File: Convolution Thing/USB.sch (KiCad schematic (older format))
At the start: 4 parts

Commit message: Added gate inputs and CM4 / display sockets, made CV inputs 100k, lots of smaller changes. First iteration of schematic now done.
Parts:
- removed J?: USB_C_Receptacle_USB2.0, symbol Connector:USB_C_Receptacle_USB2.0
- removed R? (x2): 56k, symbol Device:R
- added C?: 100nF, symbol Device:C
- added J?: USB_A, symbol Connector:USB_A
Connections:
- net labels removed: CC1, CC2
- wire segments 8 -> 4
- no-connect marks 2 -> 0
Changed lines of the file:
@@
 $Descr A4 11693 8268
 encoding utf-8
-Sheet 11 11
+Sheet 11 13
 Title ""
 Date ""
@@
 	1    0    0    -1
 $EndComp
-$Comp
-L Connector:USB_C_Receptacle_USB2.0 J?
-U 1 1 6120E9FA
-P 1400 2700
-F 0 "J?" H 1507 3567 50  0000 C CNN
-F 1 "USB_C_Receptacle_USB2.0" H 1507 3476 50  0000 C CNN
-F 2 "" H 1550 2700 50  0001 C CNN
-F 3 "https://www.usb.org/sites/default/files/documents/usb_type-c.zip" H 1550 2700 50  0001 C CNN
-	1    1400 2700
-	1    0    0    -1
-$EndComp
-$Comp
-L power:GND #PWR?
-U 1 1 61212A3C
-P 1400 3600
-F 0 "#PWR?" H 1400 3350 50  0001 C CNN
-F 1 "GND" H 1405 3427 50  0000 C CNN
-F 2 "" H 1400 3600 50  0001 C CNN
-F 3 "" H 1400 3600 50  0001 C CNN
-	1    1400 3600
-	1    0    0    -1
-$EndComp
-$Comp
-L power:GND #PWR?
-U 1 1 61213DAD
-P 1100 3600
-F 0 "#PWR?" H 1100 3350 50  0001 C CNN
-F 1 "GND" H 1105 3427 50  0000 C CNN
-F 2 "" H 1100 3600 50  0001 C CNN
-F 3 "" H 1100 3600 50  0001 C CNN
-	1    1100 3600
-	1    0    0    -1
-$EndComp
 Text Label 1800 1200 0    50   ~ 0
 USB_N
 Text Label 1800 1300 0    50   ~ 0
 USB_P
-Wire Wire Line
-	2000 2700 2000 2600
-Wire Wire Line
-	2000 2800 2000 2900
-Text Label 2100 2600 0    50   ~ 0
-USB_N
-Wire Wire Line
-	2100 2600 2000 2600
-Connection ~ 2000 2600
-Text Label 2100 2800 0    50   ~ 0
-USB_P
-Wire Wire Line
-	2100 2800 2000 2800
-Connection ~ 2000 2800
-Text Label 2000 2100 0    50   ~ 0
-VBUS
-Text Label 3200 1500 0    50   ~ 0
+Text Label 3250 1000 2    50   ~ 0
 VBUS
 $Comp
 L power:+5V #PWR?
 U 1 1 61219689
-P 3200 1100
-F 0 "#PWR?" H 3200 950 50  0001 C CNN
-F 1 "+5V" H 3215 1273 50  0000 C CNN
-F 2 "" H 3200 1100 50  0001 C CNN
-F 3 "" H 3200 1100 50  0001 C CNN
-	1    3200 1100
-	1    0    0    -1
-$EndComp
-Text Label 2000 2300 0    50   ~ 0
-CC1
-Text Label 2000 2400 0    50   ~ 0
-CC2
-Text Label 3650 1500 0    50   ~ 0
-CC1
-$Comp
-L Device:R R?
-U 1 1 6121C44A
-P 3650 1250
-F 0 "R?" H 3720 1296 50  0000 L CNN
-F 1 "56k" V 3650 1200 50  0000 L CNN
-F 2 "" V 3580 1250 50  0001 C CNN
-F 3 "~" H 3650 1250 50  0001 C CNN
-	1    3650 1250
+P 3650 1000
+F 0 "#PWR?" H 3650 850 50  0001 C CNN
+F 1 "+5V" H 3665 1173 50  0000 C CNN
+F 2 "" H 3650 1000 50  0001 C CNN
+F 3 "" H 3650 1000 50  0001 C CNN
+	1    3650 1000
 	1    0    0    -1
 $EndComp
 Wire Wire Line
-	3650 1500 3650 1400
-Wire Wire Line
 	2750 1000 2750 1400
-Wire Wire Line
-	3200 1100 3200 1500
 $Comp
-L power:+5V #PWR?
-U 1 1 6121D644
-P 3650 1100
-F 0 "#PWR?" H 3650 950 50  0001 C CNN
-F 1 "+5V" H 3665 1273 50  0000 C CNN
-F 2 "" H 3650 1100 50  0001 C CNN
-F 3 "" H 3650 1100 50  0001 C CNN
-	1    3650 1100
+L Connector:USB_A J?
+U 1 1 610E4AAF
+P 1200 2300
+F 0 "J?" H 1257 2767 50  0000 C CNN
+F 1 "USB_A" H 1257 2676 50  0000 C CNN
+F 2 "" H 1350 2250 50  0001 C CNN
+F 3 " ~" H 1350 2250 50  0001 C CNN
+	1    1200 2300
 	1    0    0    -1
 $EndComp
-Text Label 4100 1500 0    50   ~ 0
-CC2
+Text Label 1500 2100 0    50   ~ 0
+VBUS
+Text Label 1500 2300 0    50   ~ 0
+USB_P
+Text Label 1500 2400 0    50   ~ 0
+USB_N
 $Comp
-L Device:R R?
-U 1 1 6121EAE8
-P 4100 1250
-F 0 "R?" H 4170 1296 50  0000 L CNN
-F 1 "56k" V 4100 1200 50  0000 L CNN
-F 2 "" V 4030 1250 50  0001 C CNN
-F 3 "~" H 4100 1250 50  0001 C CNN
-	1    4100 1250
+L power:GND #PWR?
+U 1 1 610E6611
+P 1200 2700
+F 0 "#PWR?" H 1200 2450 50  0001 C CNN
+F 1 "GND" H 1205 2527 50  0000 C CNN
+F 2 "" H 1200 2700 50  0001 C CNN
+F 3 "" H 1200 2700 50  0001 C CNN
+	1    1200 2700
 	1    0    0    -1
 $EndComp
 Wire Wire Line
-	4100 1500 4100 1400
+	1200 2700 1100 2700
+Connection ~ 1200 2700
 $Comp
-L power:+5V #PWR?
-U 1 1 6121EAEF
-P 4100 1100
-F 0 "#PWR?" H 4100 950 50  0001 C CNN
-F 1 "+5V" H 4115 1273 50  0000 C CNN
-F 2 "" H 4100 1100 50  0001 C CNN
-F 3 "" H 4100 1100 50  0001 C CNN
-	1    4100 1100
+L Device:C C?
+U 1 1 612D057E
+P 3450 1150
+F 0 "C?" H 3565 1196 50  0000 L CNN
+F 1 "100nF" H 3565 1105 50  0000 L CNN
+F 2 "" H 3488 1000 50  0001 C CNN
+F 3 "~" H 3450 1150 50  0001 C CNN
+	1    3450 1150
 	1    0    0    -1
 $EndComp
-NoConn ~ 2000 3200
-NoConn ~ 2000 3300
+Wire Wire Line
+	3450 1000 3650 1000
+Wire Wire Line
+	3450 1000 3250 1000
+Connection ~ 3450 1000
+$Comp
+L power:GND #PWR?
+U 1 1 612D0E27
+P 3450 1300
+F 0 "#PWR?" H 3450 1050 50  0001 C CNN
+F 1 "GND" H 3455 1127 50  0000 C CNN
+F 2 "" H 3450 1300 50  0001 C CNN
+F 3 "" H 3450 1300 50  0001 C CNN
+	1    3450 1300
+	1    0    0    -1
+$EndComp
 $EndSCHEMATC

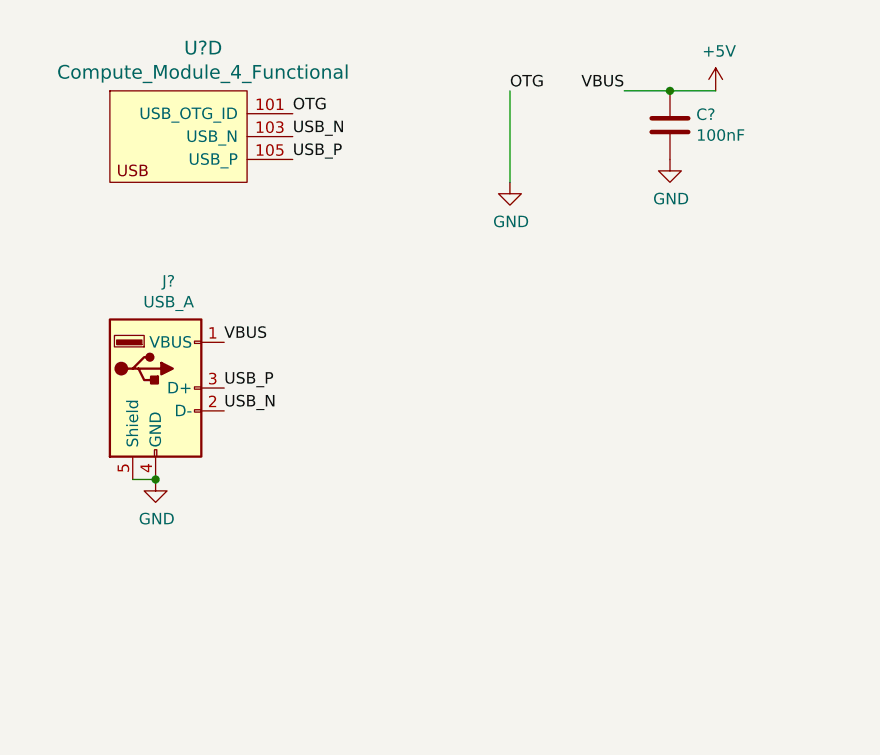
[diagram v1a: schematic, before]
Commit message: Fix some issues, add component references
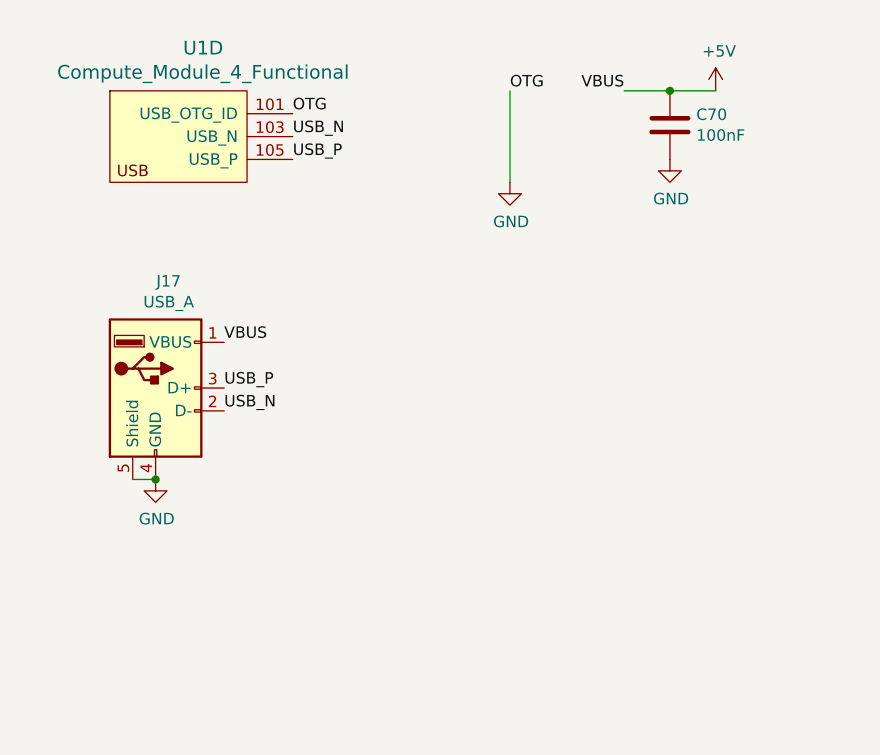
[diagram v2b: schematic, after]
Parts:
- gave numbers to parts that had none: 3
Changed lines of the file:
@@
 $EndDescr
 $Comp
-L CM4:Compute_Module_4_Functional U?
+L CM4:Compute_Module_4_Functional U1
 U 4 1 61202175
 P 800 1100
-F 0 "U?" H 1408 1387 60  0000 C CNN
+F 0 "U1" H 1408 1387 60  0000 C CNN
 F 1 "Compute_Module_4_Functional" H 1408 1281 60  0000 C CNN
 F 2 "" H 1000 1150 60  0001 L CNN
@@
 OTG
 $Comp
-L power:GND #PWR?
+L power:GND #PWR0127
 U 1 1 6120C5F8
 P 2750 1400
-F 0 "#PWR?" H 2750 1150 50  0001 C CNN
+F 0 "#PWR0127" H 2750 1150 50  0001 C CNN
 F 1 "GND" H 2755 1227 50  0000 C CNN
 F 2 "" H 2750 1400 50  0001 C CNN
@@
 VBUS
 $Comp
-L power:+5V #PWR?
+L power:+5V #PWR0129
 U 1 1 61219689
 P 3650 1000
-F 0 "#PWR?" H 3650 850 50  0001 C CNN
+F 0 "#PWR0129" H 3650 850 50  0001 C CNN
 F 1 "+5V" H 3665 1173 50  0000 C CNN
 F 2 "" H 3650 1000 50  0001 C CNN
@@
 	2750 1000 2750 1400
 $Comp
-L Connector:USB_A J?
+L Connector:USB_A J17
 U 1 1 610E4AAF
 P 1200 2300
-F 0 "J?" H 1257 2767 50  0000 C CNN
+F 0 "J17" H 1257 2767 50  0000 C CNN
 F 1 "USB_A" H 1257 2676 50  0000 C CNN
 F 2 "" H 1350 2250 50  0001 C CNN
@@
 USB_N
 $Comp
-L power:GND #PWR?
+L power:GND #PWR0126
 U 1 1 610E6611
 P 1200 2700
-F 0 "#PWR?" H 1200 2450 50  0001 C CNN
+F 0 "#PWR0126" H 1200 2450 50  0001 C CNN
 F 1 "GND" H 1205 2527 50  0000 C CNN
 F 2 "" H 1200 2700 50  0001 C CNN
@@
 Connection ~ 1200 2700
 $Comp
-L Device:C C?
+L Device:C C70
 U 1 1 612D057E
 P 3450 1150
-F 0 "C?" H 3565 1196 50  0000 L CNN
+F 0 "C70" H 3565 1196 50  0000 L CNN
 F 1 "100nF" H 3565 1105 50  0000 L CNN
 F 2 "" H 3488 1000 50  0001 C CNN
@@
 Connection ~ 3450 1000
 $Comp
-L power:GND #PWR?
+L power:GND #PWR0128
 U 1 1 612D0E27
 P 3450 1300
-F 0 "#PWR?" H 3450 1050 50  0001 C CNN
+F 0 "#PWR0128" H 3450 1050 50  0001 C CNN
 F 1 "GND" H 3455 1127 50  0000 C CNN
 F 2 "" H 3450 1300 50  0001 C CNN

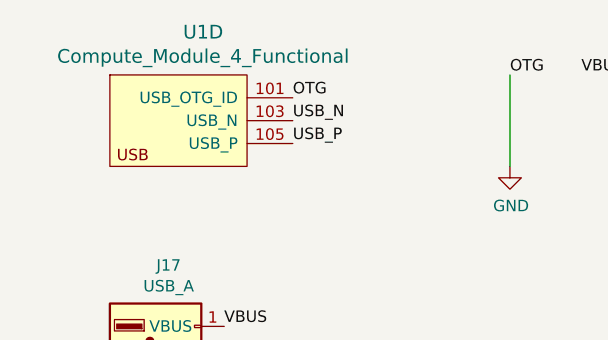
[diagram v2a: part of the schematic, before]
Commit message: Started footprint assignment
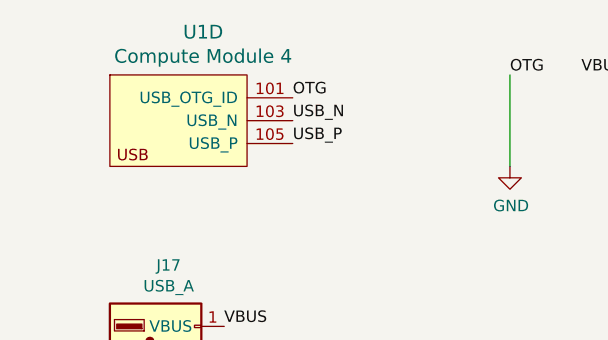
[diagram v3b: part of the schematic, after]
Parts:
- U1: value Compute_Module_4_Functional -> Compute Module 4; footprint (none) -> CM4:Raspberry-Pi-4-Compute-Module
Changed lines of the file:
@@
 P 800 1100
 F 0 "U1" H 1408 1387 60  0000 C CNN
-F 1 "Compute_Module_4_Functional" H 1408 1281 60  0000 C CNN
-F 2 "" H 1000 1150 60  0001 L CNN
+F 1 "Compute Module 4" H 1408 1281 60  0000 C CNN
+F 2 "CM4:Raspberry-Pi-4-Compute-Module" H 1000 1150 60  0001 L CNN
 F 3 "" H 1000 950 60  0001 L CNN
 	4    800  1100

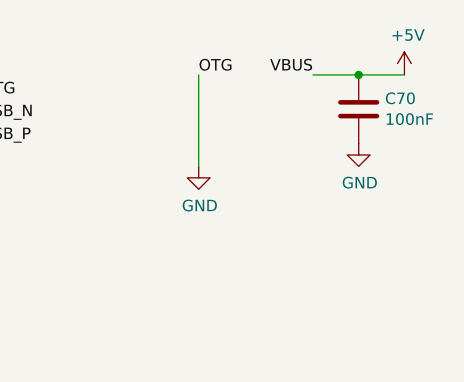
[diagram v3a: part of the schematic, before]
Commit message: Assign all footprints
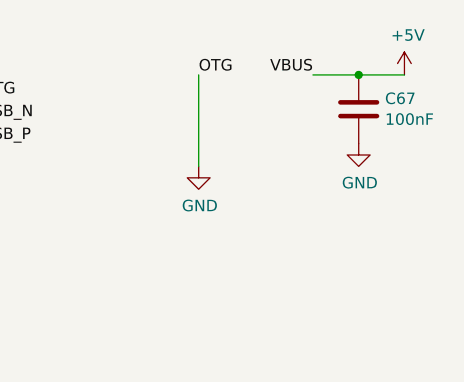
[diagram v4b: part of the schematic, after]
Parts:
- C67: renamed from C70; footprint (none) -> Capacitor_SMD:C_0805_2012Metric
- J17: footprint (none) -> Connector_USB:USB_A_Molex_105057_Vertical
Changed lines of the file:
@@
 OTG
 $Comp
-L power:GND #PWR0127
+L power:GND #PWR0120
 U 1 1 6120C5F8
 P 2750 1400
-F 0 "#PWR0127" H 2750 1150 50  0001 C CNN
+F 0 "#PWR0120" H 2750 1150 50  0001 C CNN
 F 1 "GND" H 2755 1227 50  0000 C CNN
 F 2 "" H 2750 1400 50  0001 C CNN
@@
 VBUS
 $Comp
-L power:+5V #PWR0129
+L power:+5V #PWR0122
 U 1 1 61219689
 P 3650 1000
-F 0 "#PWR0129" H 3650 850 50  0001 C CNN
+F 0 "#PWR0122" H 3650 850 50  0001 C CNN
 F 1 "+5V" H 3665 1173 50  0000 C CNN
 F 2 "" H 3650 1000 50  0001 C CNN
@@
 F 0 "J17" H 1257 2767 50  0000 C CNN
 F 1 "USB_A" H 1257 2676 50  0000 C CNN
-F 2 "" H 1350 2250 50  0001 C CNN
+F 2 "Connector_USB:USB_A_Molex_105057_Vertical" H 1350 2250 50  0001 C CNN
 F 3 " ~" H 1350 2250 50  0001 C CNN
 	1    1200 2300
@@
 USB_N
 $Comp
-L power:GND #PWR0126
+L power:GND #PWR0119
 U 1 1 610E6611
 P 1200 2700
-F 0 "#PWR0126" H 1200 2450 50  0001 C CNN
+F 0 "#PWR0119" H 1200 2450 50  0001 C CNN
 F 1 "GND" H 1205 2527 50  0000 C CNN
 F 2 "" H 1200 2700 50  0001 C CNN
@@
 Connection ~ 1200 2700
 $Comp
-L Device:C C70
+L Device:C C67
 U 1 1 612D057E
 P 3450 1150
-F 0 "C70" H 3565 1196 50  0000 L CNN
+F 0 "C67" H 3565 1196 50  0000 L CNN
 F 1 "100nF" H 3565 1105 50  0000 L CNN
-F 2 "" H 3488 1000 50  0001 C CNN
+F 2 "Capacitor_SMD:C_0805_2012Metric" H 3488 1000 50  0001 C CNN
 F 3 "~" H 3450 1150 50  0001 C CNN
 	1    3450 1150
@@
 Connection ~ 3450 1000
 $Comp
-L power:GND #PWR0128
+L power:GND #PWR0121
 U 1 1 612D0E27
 P 3450 1300
-F 0 "#PWR0128" H 3450 1050 50  0001 C CNN
+F 0 "#PWR0121" H 3450 1050 50  0001 C CNN
 F 1 "GND" H 3455 1127 50  0000 C CNN
 F 2 "" H 3450 1300 50  0001 C CNN

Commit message: PCB layout work and related changes to the schematic
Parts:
- removed U1: Compute Module 4, CM4:Raspberry-Pi-4-Compute-Module, symbol CM4:Compute_Module_4_Functional
- renumbered C67 to C64, J17 to J15
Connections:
- net USB_N renamed CM4_USB_N
- net USB_P renamed CM4_USB_P
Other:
- moved on the sheet: C64, J15
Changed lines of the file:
@@
 $Descr A4 11693 8268
 encoding utf-8
-Sheet 11 13
+Sheet 10 13
 Title ""
 Date ""
@@
 Comment4 ""
 $EndDescr
+Text Label 1850 1050 2    50   ~ 0
+VBUS
 $Comp
-L CM4:Compute_Module_4_Functional U1
-U 4 1 61202175
-P 800 1100
-F 0 "U1" H 1408 1387 60  0000 C CNN
-F 1 "Compute Module 4" H 1408 1281 60  0000 C CNN
-F 2 "CM4:Raspberry-Pi-4-Compute-Module" H 1000 1150 60  0001 L CNN
-F 3 "" H 1000 950 60  0001 L CNN
-	4    800  1100
+L power:+5V #PWR0112
+U 1 1 61219689
+P 2250 1050
+F 0 "#PWR0112" H 2250 900 50  0001 C CNN
+F 1 "+5V" H 2265 1223 50  0000 C CNN
+F 2 "" H 2250 1050 50  0001 C CNN
+F 3 "" H 2250 1050 50  0001 C CNN
+	1    2250 1050
 	1    0    0    -1
 $EndComp
-Text Label 1800 1100 0    50   ~ 0
-OTG
-Text Label 2750 1000 0    50   ~ 0
-OTG
 $Comp
-L power:GND #PWR0120
-U 1 1 6120C5F8
-P 2750 1400
-F 0 "#PWR0120" H 2750 1150 50  0001 C CNN
-F 1 "GND" H 2755 1227 50  0000 C CNN
-F 2 "" H 2750 1400 50  0001 C CNN
-F 3 "" H 2750 1400 50  0001 C CNN
-	1    2750 1400
+L Connector:USB_A J15
+U 1 1 610E4AAF
+P 950 1200
+F 0 "J15" H 1007 1667 50  0000 C CNN
+F 1 "USB_A" H 1007 1576 50  0000 C CNN
+F 2 "Connector_USB:USB_A_Molex_105057_Vertical" H 1100 1150 50  0001 C CNN
+F 3 " ~" H 1100 1150 50  0001 C CNN
+	1    950  1200
 	1    0    0    -1
 $EndComp
-Text Label 1800 1200 0    50   ~ 0
-USB_N
-Text Label 1800 1300 0    50   ~ 0
-USB_P
-Text Label 3250 1000 2    50   ~ 0
+Text Label 1250 1000 0    50   ~ 0
 VBUS
 $Comp
-L power:+5V #PWR0122
-U 1 1 61219689
-P 3650 1000
-F 0 "#PWR0122" H 3650 850 50  0001 C CNN
-F 1 "+5V" H 3665 1173 50  0000 C CNN
-F 2 "" H 3650 1000 50  0001 C CNN
-F 3 "" H 3650 1000 50  0001 C CNN
-	1    3650 1000
+L power:GND #PWR0110
+U 1 1 610E6611
+P 950 1600
+F 0 "#PWR0110" H 950 1350 50  0001 C CNN
+F 1 "GND" H 955 1427 50  0000 C CNN
+F 2 "" H 950 1600 50  0001 C CNN
+F 3 "" H 950 1600 50  0001 C CNN
+	1    950  1600
 	1    0    0    -1
 $EndComp
 Wire Wire Line
-	2750 1000 2750 1400
+	950  1600 850  1600
+Connection ~ 950  1600
 $Comp
-L Connector:USB_A J17
-U 1 1 610E4AAF
-P 1200 2300
-F 0 "J17" H 1257 2767 50  0000 C CNN
-F 1 "USB_A" H 1257 2676 50  0000 C CNN
-F 2 "Connector_USB:USB_A_Molex_105057_Vertical" H 1350 2250 50  0001 C CNN
-F 3 " ~" H 1350 2250 50  0001 C CNN
-	1    1200 2300
-	1    0    0    -1
-$EndComp
-Text Label 1500 2100 0    50   ~ 0
-VBUS
-Text Label 1500 2300 0    50   ~ 0
-USB_P
-Text Label 1500 2400 0    50   ~ 0
-USB_N
-$Comp
-L power:GND #PWR0119
-U 1 1 610E6611
-P 1200 2700
-F 0 "#PWR0119" H 1200 2450 50  0001 C CNN
-F 1 "GND" H 1205 2527 50  0000 C CNN
-F 2 "" H 1200 2700 50  0001 C CNN
-F 3 "" H 1200 2700 50  0001 C CNN
-	1    1200 2700
+L Device:C C64
+U 1 1 612D057E
+P 2050 1200
+F 0 "C64" H 2165 1246 50  0000 L CNN
+F 1 "100nF" H 2165 1155 50  0000 L CNN
+F 2 "Capacitor_SMD:C_0805_2012Metric" H 2088 1050 50  0001 C CNN
+F 3 "~" H 2050 1200 50  0001 C CNN
+	1    2050 1200
 	1    0    0    -1
 $EndComp
 Wire Wire Line
-	1200 2700 1100 2700
-Connection ~ 1200 2700
+	2050 1050 2250 1050
+Wire Wire Line
+	2050 1050 1850 1050
+Connection ~ 2050 1050
 $Comp
-L Device:C C67
-U 1 1 612D057E
-P 3450 1150
-F 0 "C67" H 3565 1196 50  0000 L CNN
-F 1 "100nF" H 3565 1105 50  0000 L CNN
-F 2 "Capacitor_SMD:C_0805_2012Metric" H 3488 1000 50  0001 C CNN
-F 3 "~" H 3450 1150 50  0001 C CNN
-	1    3450 1150
+L power:GND #PWR0111
+U 1 1 612D0E27
+P 2050 1350
+F 0 "#PWR0111" H 2050 1100 50  0001 C CNN
+F 1 "GND" H 2055 1177 50  0000 C CNN
+F 2 "" H 2050 1350 50  0001 C CNN
+F 3 "" H 2050 1350 50  0001 C CNN
+	1    2050 1350
 	1    0    0    -1
 $EndComp
-Wire Wire Line
-	3450 1000 3650 1000
-Wire Wire Line
-	3450 1000 3250 1000
-Connection ~ 3450 1000
-$Comp
-L power:GND #PWR0121
-U 1 1 612D0E27
-P 3450 1300
-F 0 "#PWR0121" H 3450 1050 50  0001 C CNN
-F 1 "GND" H 3455 1127 50  0000 C CNN
-F 2 "" H 3450 1300 50  0001 C CNN
-F 3 "" H 3450 1300 50  0001 C CNN
-	1    3450 1300
-	1    0    0    -1
-$EndComp
+Text GLabel 1250 1300 2    50   BiDi ~ 0
+CM4_USB_N
+Text GLabel 1250 1200 2    50   BiDi ~ 0
+CM4_USB_P
 $EndSCHEMATC
